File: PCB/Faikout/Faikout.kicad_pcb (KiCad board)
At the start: 2 copper layers, 70 x 70 mm, 47 parts, among them J1 1x5, J2 TC2030-USB-NL, J3 Reset, Q1 BSS138PS, U1 TPS562246, U4 ESP32-S3-MINI-1-N4R2

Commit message: Tidy for order
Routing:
- net Net-(D4-K): track 33.7 -> 34.6 mm

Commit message: For order
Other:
- board text added: "E"

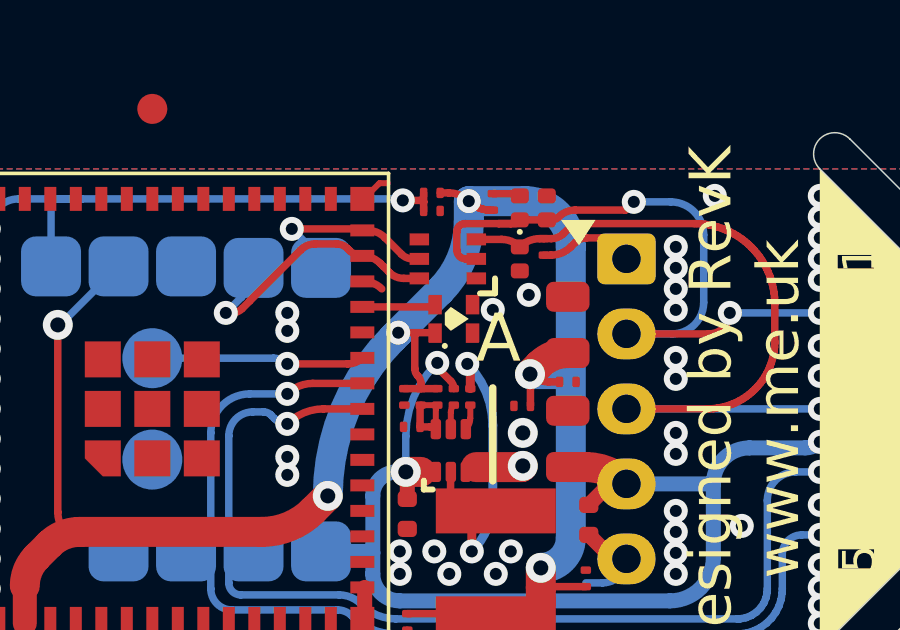
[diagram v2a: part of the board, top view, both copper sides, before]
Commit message: LED loop for ATE
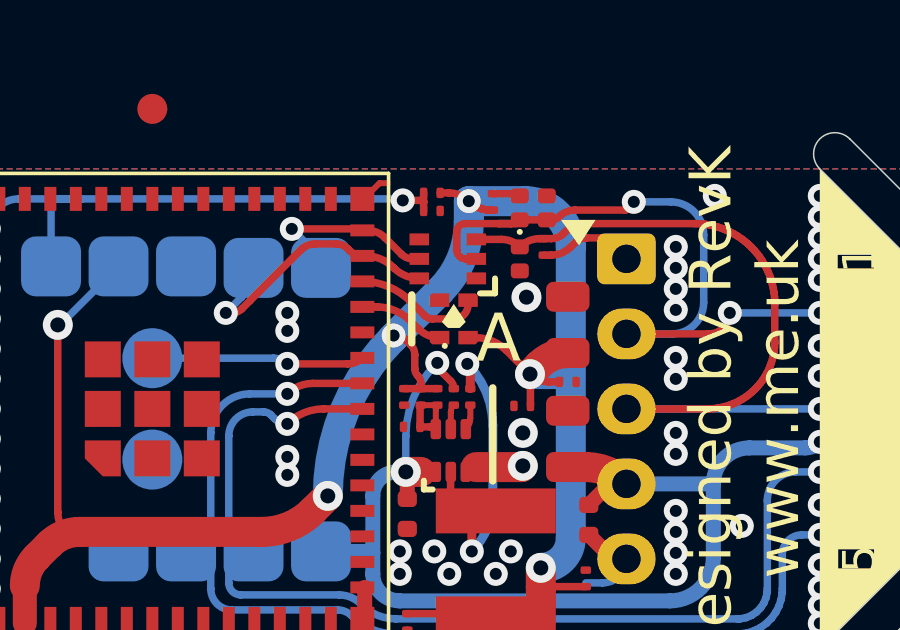
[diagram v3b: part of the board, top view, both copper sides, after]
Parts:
- D1: footprint RevK:SMD1615-Blind -> RevK:SMD1615
- U4: value ESP32-S3-MINI-1-N4R2 -> ESP32-S3-MINI-1
- turned D1 to -90 degrees
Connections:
- D1 pad 4: unconnected-(D1-O-Pad4) -> LEDO
- U4 pad 28: GND -> LEDO
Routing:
- net LEDO: track 0.00 -> 4.32 mm
- net +3.3V: track 65.2 -> 66.6 mm
- net GND: track 7.68 -> 7.01 mm, vias 52 -> 51

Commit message: Silkscreen fix
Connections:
- D1 pad 2: LED -> LEDO
- D1 pad 4: LEDO -> LEDI
- U4 pad 27: LED -> LEDO
- U4 pad 28: LEDO -> LEDI
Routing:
- net LEDI: track 0.00 -> 4.32 mm
- net LED: track 2.88 -> 0.00 mm
- net LEDO: track 4.32 -> 2.88 mm
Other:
- board text added: "33"
- board text added: "LED"

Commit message: footprint tidy
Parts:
- U1: footprint RevK:SOT-563 -> RevK:SOT-5x3-6

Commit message: Vias
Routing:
- net GND: vias 51 -> 72
